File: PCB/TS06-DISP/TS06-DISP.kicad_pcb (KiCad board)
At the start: 2 copper layers, 176 x 44 mm, 30 parts

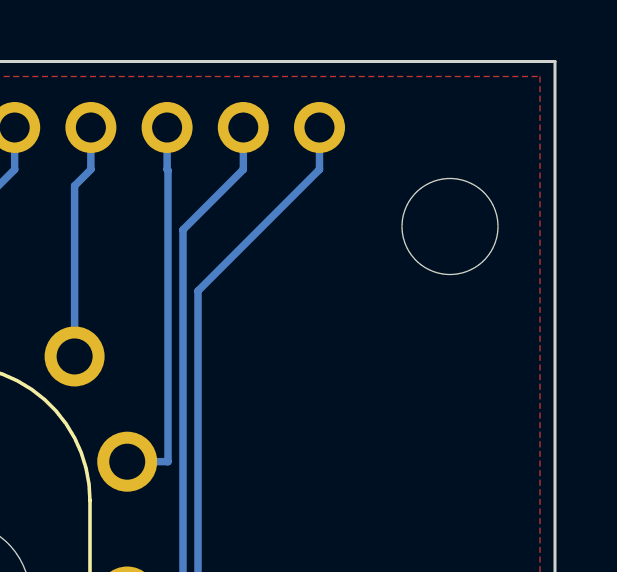
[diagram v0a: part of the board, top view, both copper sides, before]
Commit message: Pair: move the top-right standoff clear of XP12; review corrected by an independent check
The display's H4 standoff shares the gap between the boards with XP12's plastic body. No
courtyard check compares them, because the hole's footprint is on the front and the strip's
on the back. At (172.5, 5.5) a hex spacer's corner came 0.5 mm from the strip's end. It now
sits at (172.5, 7.5) on both boards: 1.9 mm to a 5.5 mm hex, 1.6 mm to a 7 mm washer. The
display's copper is unchanged. TS06-DISP: 0 vias, checkcopper --hv clean. KiCad 10 DRC shows
0 unconnected and only the two known colon courtyard overlaps. TS06-DRV takes the new hole
when it is regenerated from its route.

The review and the generator's comments are corrected where an independent audit found them
wrong:
- R21-R26 are the opto LEDs' resistors, not anode resistors.
- There are three IC orientations, not four.
- Only H3 is between tubes.
- The colon overlap is 0.135 mm.
- The inside depth is 64-71 mm.
- The Nano's fan-out is hand-laid.

Co-Authored-By: Claude Opus 5.5 <noreply@anthropic.com>
Claude-Session: https://claude.ai/code/session_01WoV3gyAFgmtuk6W6Dr4bdA
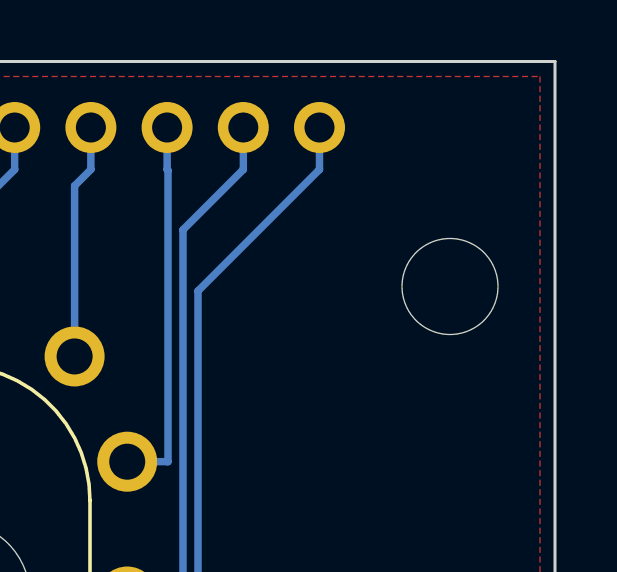
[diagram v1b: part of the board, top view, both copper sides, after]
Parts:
- moved H4 2.00 mm to (172.5, 7.50)
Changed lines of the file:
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@@
 	(footprint "TS06:TS06_MountingHole_M3"
 		(layer "F.Cu")
-		(at 172.5 5.5)
+		(at 172.5 7.5)
 		(descr "Mounting Hole 3.2mm, M3, no annular, generated by kicad-footprint-generator mountinghole.py. Copied from KiCad 10.0.6's stock library (MountingHole_3.2mm_M3): the standoff holes of the TERMINAL-06 THT board pair.")
 		(tags "mountinghole M3")

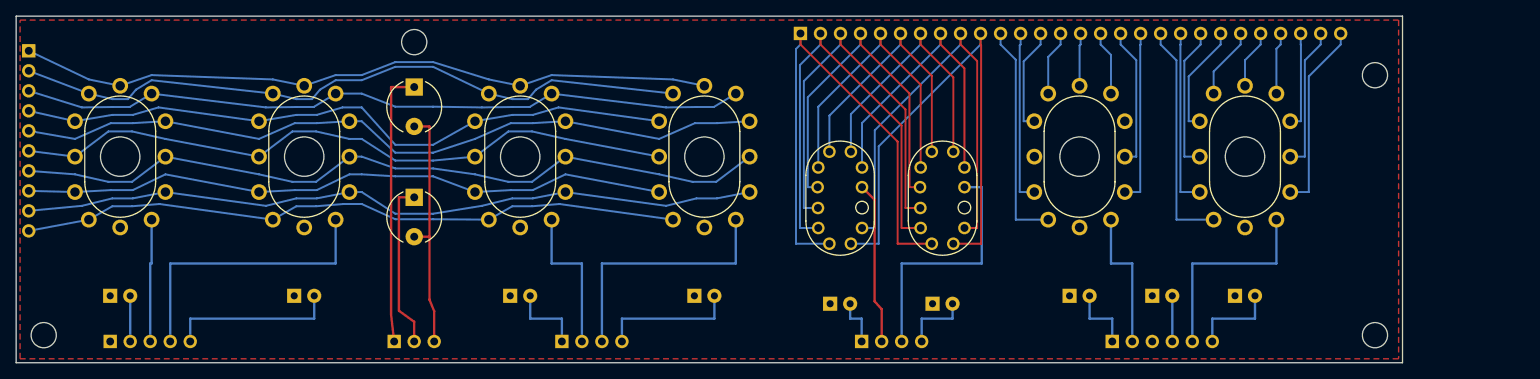
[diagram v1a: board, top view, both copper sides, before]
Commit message: Pair: the seconds pair re-spaced to 20.5 for its Ø20 stems; boards widened to 191.4
The owner chose to widen the boards and keep the Gyver pitch. Where things now are:
- TS06-DISP:
  - The ИН-12s and the colon are where they were.
  - S10 and S1 stand 20.5 apart (was 13.0), each stem 2.2 mm from the glass beside it. That
    spacing is concept Rev F's, from the tube's outline drawing.
  - The ИН-15 pair moved 15.4 right. The board is 191.4 x 44.
  - The ИН-17 bundles are set from each tube's centre, and their order is unchanged, so no line
    crosses another.
  - XP12 is still one strip: 31 pins, with three spares between the ИН-17 group (moved 7.78)
    and the ИН-15 group (moved 15.4).
  - Checks: 0 vias; checkcopper --hv clean; audit clean; KiCad 10 DRC 0 unconnected, with only
    the known colon overlaps.
- ts06pair: HEADERS['12'] has the three spare pins. There are stock 1x31 PLS/PBS footprints.
- mkpcb_drv:
  - Parts behind the ИН-17 group move 7.62 mm and parts behind the ИН-12s, with the Nano, U2
    and the lines between them, 15.4 mm. The ИН-15 side stays put.
  - check_mate() == [], and the hand-laid copper is clean.
  - The old route no longer fits the board, so it is removed. TS06-DRV is being re-routed and
    its board file is the previous one until then.
- The case model (3d/case-pair) re-reads both boards. The ИН-17 check now computes its own
  verdict: TIGHT, 0.5 stem to stem. The case is 204.4 mm wide, Rev F's face width.

Co-Authored-By: Claude Opus 5.5 <noreply@anthropic.com>
Claude-Session: https://claude.ai/code/session_01WoV3gyAFgmtuk6W6Dr4bdA
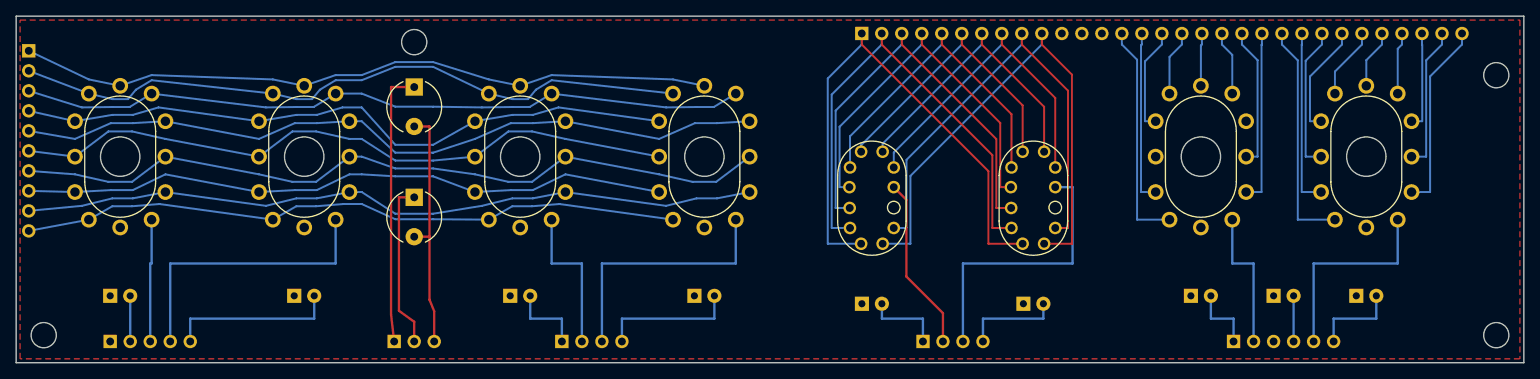
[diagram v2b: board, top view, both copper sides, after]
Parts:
- XP12: value PLS-28 male 2.54 -> PLS-31 male 2.54; footprint TS06:TS06_PinHeader_1x28_R90 -> TS06:TS06_PinHeader_1x31_R90
- moved H2 15.4 mm to (187.9, 40.5)
- moved H4 15.4 mm to (187.9, 7.50)
- moved HL7 15.4 mm to (150.4, 35.5)
- moved HL8 15.4 mm to (171.4, 35.5)
- moved HL9 15.4 mm to (160.9, 35.5)
- moved V10 15.4 mm to (171.4, 17.8)
- moved V9 15.4 mm to (150.4, 17.8)
- moved XP25 15.4 mm to (154.6, 41.3)
- moved HL6 11.5 mm to (129.1, 36.5)
- moved V6 11.5 mm to (129.1, 23.2)
- moved XP12 7.78 mm to (107.3, 2.20)
- moved XP24 7.78 mm to (115.1, 41.3)
- moved HL5 4.03 mm to (108.6, 36.5)
- moved V5 4.03 mm to (108.6, 23.2)
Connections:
- XP12 pad 11: CAT_B_AMP -> (no net)
- XP12 pad 12: CAT_B_OHM -> (no net)
- XP12 pad 13: CAT_B_SIEMENS -> (no net)
- XP12 pad 14: CAT_B_VOLT -> CAT_B_AMP
- XP12 pad 15: CAT_B_HENRY -> CAT_B_OHM
- XP12 pad 16: CAT_B_HERTZ -> CAT_B_SIEMENS
- XP12 pad 17: CAT_B_FARAD -> CAT_B_VOLT
- XP12 pad 18: CAT_B_WATT -> CAT_B_HENRY
- XP12 pad 19: CAT_A_NANO -> CAT_B_HERTZ
- XP12 pad 20: CAT_A_PCT -> CAT_B_FARAD
- XP12 pad 21: CAT_A_PI -> CAT_B_WATT
- XP12 pad 22: CAT_A_KILO -> CAT_A_NANO
- XP12 pad 23: CAT_A_MEGA -> CAT_A_PCT
- XP12 pad 24: CAT_A_MILLI -> CAT_A_PI
- XP12 pad 25: CAT_A_PLUS -> CAT_A_KILO
- XP12 pad 26: CAT_A_MINUS -> CAT_A_MEGA
- XP12 pad 27: CAT_A_P -> CAT_A_MILLI
- XP12 pad 28: CAT_A_MICRO -> CAT_A_PLUS
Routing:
- net ANODE_S1: track 32.0 -> 35.7 mm
- net BL_A6: track 8.71 -> 12.5 mm
- net BL_A5: track 6.25 -> 10.0 mm
- net KS9: track 58.0 -> 61.1 mm
- net KS6: track 59.5 -> 62.6 mm
- net KS8: track 65.8 -> 68.9 mm
- net KS7: track 67.3 -> 70.4 mm
- net KS5: track 53.3 -> 56.4 mm
- net KS4: track 47.0 -> 50.1 mm
- net KS3: track 39.4 -> 42.5 mm
- net KS2: track 35.4 -> 38.5 mm
- net KS1: track 35.4 -> 38.5 mm
- net KS0: track 39.4 -> 42.5 mm
- net ANODE_S10: track 20.6 -> 22.2 mm
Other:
- board size 176 x 44 mm -> 191.4 x 44 mm

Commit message: TS06-DISP: A6 clearance at every 185 V pad, 0.5 at cathode pads, standoff keep-outs
From the electrical grill (E3, E10, F12):

* E3, IPC-2221B table 6-1 A6: a bare 185 V pad keeps 0.8 mm from copper of
  any other net. The generator now writes TS06-DISP.kicad_dru with the pair's
  shared rule, so KiCad's DRC and pour fill hold it: the BL_K pour moves from
  0.60 to 0.80 mm off all 23 HV pads. The rule needs "0.8mm": KiCad 10 rejects
  a unitless number, and kicad-cli then drops the whole file without a word.
  The tracks that were short moved: S10's anode jog 1.6 -> 1.85 (0.654 ->
  0.90 from V5.9); the KS9/KS8 lanes 4.395/4.895 -> 4.55/5.05 on both ИН-17
  (0.693 -> 0.85 from the anodes); the colon lines 0.69 -> 0.85 from the
  other lamp's pads; K1 leaves each ИН-12 at 15 degrees through the gap
  between K0 and the anode (0.772 -> 0.88 from the anode).
* E10: every cathode pad is at least 0.5 mm from other nets (was 0.33 at
  V1-V3's K7, 15 pads under 0.5): K5 leaves over K7's pad at 45 degrees,
  K4 and K0 run level past the pad beside them, the S10 lanes match S1's,
  and the ИН-17 lanes onto pads 3 and 0 stand 0.02 outside the pad centres.
* F12: a KiCad rule area (no tracks, vias or pour, both faces) of 3.8 mm
  radius round each standoff hole. K6 and K5 no longer cross above the
  upper colon lamp, 2.4 mm from H3; the colon crossing is re-laid as 45
  degree fans into three gaps between the lamp pads.
* The generator checks all three on its own geometry, and exits 1 if any
  check fails. Docstring: XP12's pin groups, not XP13/XP14.

388 tracks, 0 vias; checkcopper --hv, audit clean; check_mate() [].

Co-Authored-By: Claude Opus 5.5 <noreply@anthropic.com>
Claude-Session: https://claude.ai/code/session_01WoV3gyAFgmtuk6W6Dr4bdA
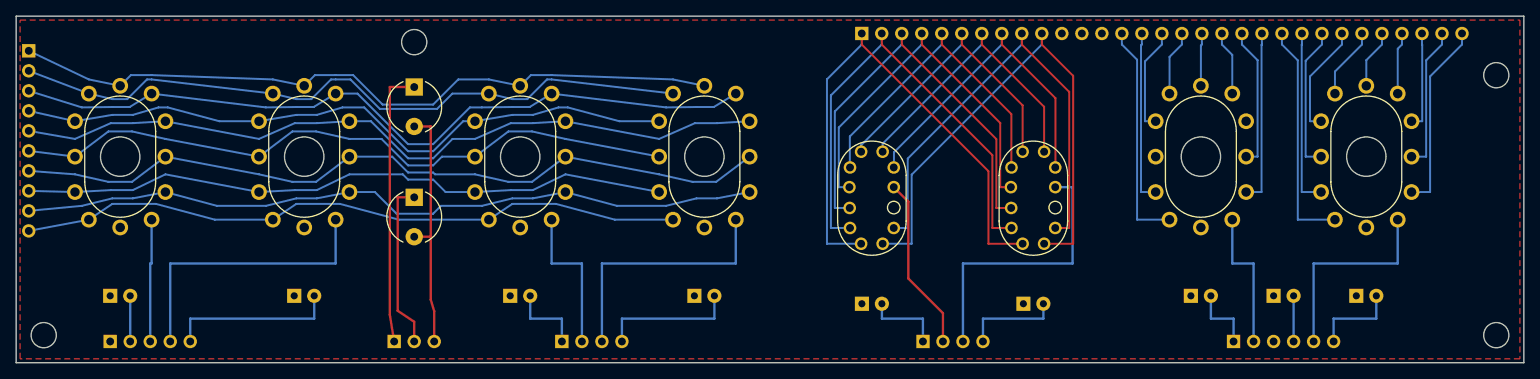
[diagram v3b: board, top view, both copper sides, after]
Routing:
- net K7: track 92.5 -> 96.8 mm
- net K6: track 88.3 -> 91.5 mm
- net K5: track 86.5 -> 88.2 mm
- net K4: track 83.9 -> 85.1 mm
- net K8: track 95.6 -> 96.7 mm
- net K3: track 84.9 -> 85.9 mm
- net K0: track 93.4 -> 94.3 mm
- net K9: track 97.0 -> 97.6 mm
- net K2: track 82.2 -> 82.8 mm
- net K1: track 84.0 -> 84.5 mm

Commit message: TS06-DISP rev B: silkscreen for white on black mask, to the fab's minimums
Rezonit and JLC alike: lines 0.15 mm, text 1.0 mm tall with a 0.15 mm stroke,
no silk on pads. The project file now sets KiCad's text minimum to 1.0/0.15
so its DRC holds it; the generator checks line widths, sizes, and text
against pads, holes, outlines and the edge, and exits 1 on a problem.

Footprints this board owns: IN12, IN17 and INS1 silk 0.12 -> 0.15 mm; the
strips' rotated variants (1x03/04/05/06_R90, 1x10_R180, 1x31_R90) are
widened as the generator writes them, the same on the board and in the
library (no lib_footprint_mismatch).

The FRONT, which the owner sees between the tubes, carries only what
fitting a part needs, mostly where the part covers it: tube names inside
each ring (H10 H1 M10 M1, S10 S1, "ИН-15Б" AM / "ИН-15А" PM - the stroke
font renders the Cyrillic), a ring round the ИН-12/ИН-15 anode pad (pin 1,
the key), the ИН-17's gap ring, a K beside each LED's square pad (the
cathode), a dot and an A beside each ИНС-1's square pad (the anode). The
bottom band, behind the fascia, says which convention is which and marks
185 V on the strip joints.

The BACK faces TS06-DRV and is where every joint is soldered: title
"TERMINAL-06 TS06-DISP rev B" with the date and "this face to TS06-DRV";
XP11-XP25 beside pin 1 (the footprint's corner mark on pin 1); both
conventions spelled out; "solder XP11-XP25 plugged into TS06-DRV"; standoff
seats and "4 x M3, 11 mm"; a 185 V warning with "unplug, wait 15 s"; the tube
names again, and the LEDs' K and the lamps' A.

KiCad 10 DRC: 0 unconnected, 0 warnings, the 2 accepted courtyard errors.

Co-Authored-By: Claude Opus 5.5 <noreply@anthropic.com>
Claude-Session: https://claude.ai/code/session_01WoV3gyAFgmtuk6W6Dr4bdA
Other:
- board text added: "!"
- board text added: "185 V"
- board text added: "30.09.26 · this face to TS06-DRV"
- board text added: "4 × M3, 11 mm"
- board text added: "A"
- board text added: "AM"
- board text added: "H1"
- board text added: "H10"
- board text added: "K"
- board text added: "LED HL1-HL9: □ pad = K (cathode)"
- board text added: "LED: □ pad = K"
- board text added: "M1"
- board text added: "M10"
- board text added: "PM"
- board text added: "S1"
- board text added: "S10"
- board text added: "TERMINAL-06 TS06-DISP rev B"
- board text added: "solder XP11-XP25 plugged into TS06-DRV"
- board text added: "standoffs"
- board text added: "unplug,"
- board text added: "wait 15 s"
- board text added: "ИН-15А"
- board text added: "ИН-15Б"
- board text added: "ИНС-1 V7 V8: □ pad = A (anode, the dot)"
- board text added: "ИНС-1: □ pad = A •"
- board text removed: "TERMINAL-06 display"
- board text removed: "TS06-DISP rev A"

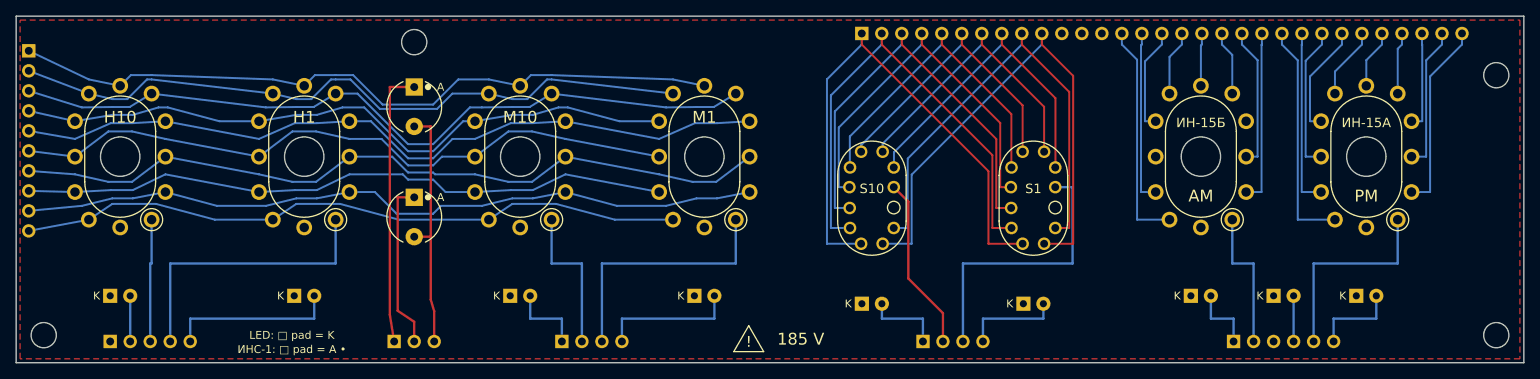
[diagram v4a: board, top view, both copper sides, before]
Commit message: TS06-DISP: the circuit-as-ornament silkscreen art is the committed board
The owner approved direction 3, "circuit" (30.09.26: "the best for display pcb is circuit as
ornament"). tools/mkpcb_disp.py now draws it by default; --art none writes plain rev B (byte for
byte the board it wrote before), and engraving and constructivist stay as options that write only
to a --out of their own. PCB/TS06-DISP/TS06-DISP.kicad_pcb regenerated with `python3 tools/mkpcb_disp.py`.

Checks: verify_pair.sh 27 PASS, 0 FAIL, 0 SKIP; KiCad 10.0.6 DRC (zones refilled, all severities)
2 errors, the 2 accepted colon courtyard overlaps of rev B (V3/V7, V3/V8), 0 warnings, 0 unconnected.
Three pin labels are left out on the back (bench-only, silk, no electrical effect): H and m, the
top-pin cathodes of the two ИН-15, under the tubes' own name labels, and A, the ampere cathode of
ИН-15Б (pin 9), beside its AM label. XP12's legend names all three.

Co-Authored-By: Claude Opus 5.5 <noreply@anthropic.com>
Claude-Session: https://claude.ai/code/session_01WoV3gyAFgmtuk6W6Dr4bdA
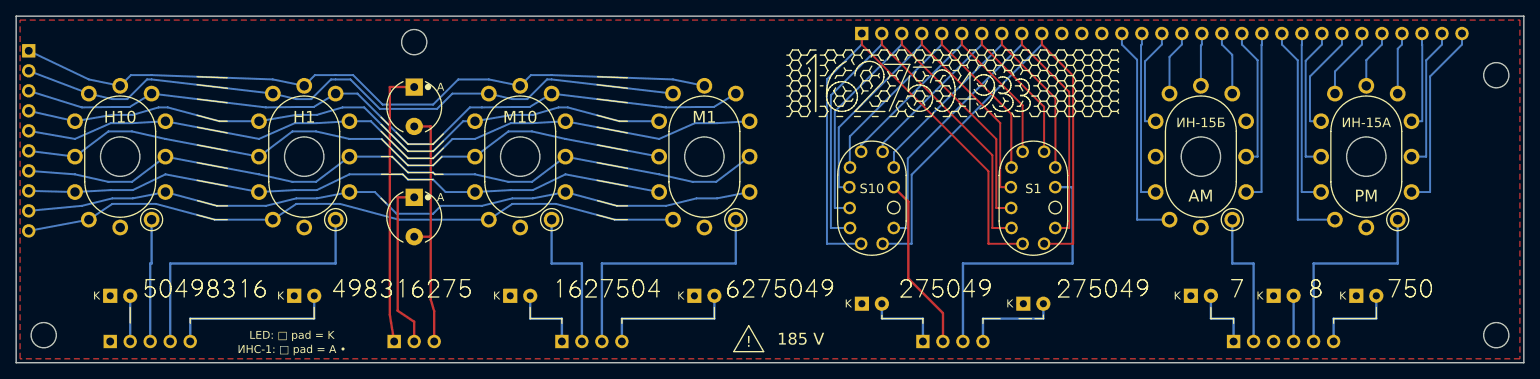
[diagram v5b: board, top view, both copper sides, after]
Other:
- board text added: "%"
- board text added: "+"
- board text added: "0"
- board text added: "1"
- board text added: "2"
- board text added: "3"
- board text added: "4"
- board text added: "5"
- board text added: "6"
- board text added: "7"
- board text added: "8"
- board text added: "9"
- board text added: "F"
- board text added: "H"
- board text added: "Hz"
- board text added: "M"
- board text added: "P"
- board text added: "S"
- board text added: "V"
- board text added: "W"
- board text added: "k"
- board text added: "m"
- board text added: "n"
- board text added: "µ"
- board text added: "Ω"
- board text added: "π"
- board text added: "−"
